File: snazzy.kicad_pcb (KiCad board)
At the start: 2 copper layers, 28 parts, among them J1 Conn_01x03, J2 Conn_01x03, SW1 BTN_START, SW10 BTN_DOWN, SW11 BTN_L, SW12 BTN_R, SW2 BTN_SELECT, SW3 BTN_A, SW4 BTN_B, SW5 BTN_X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

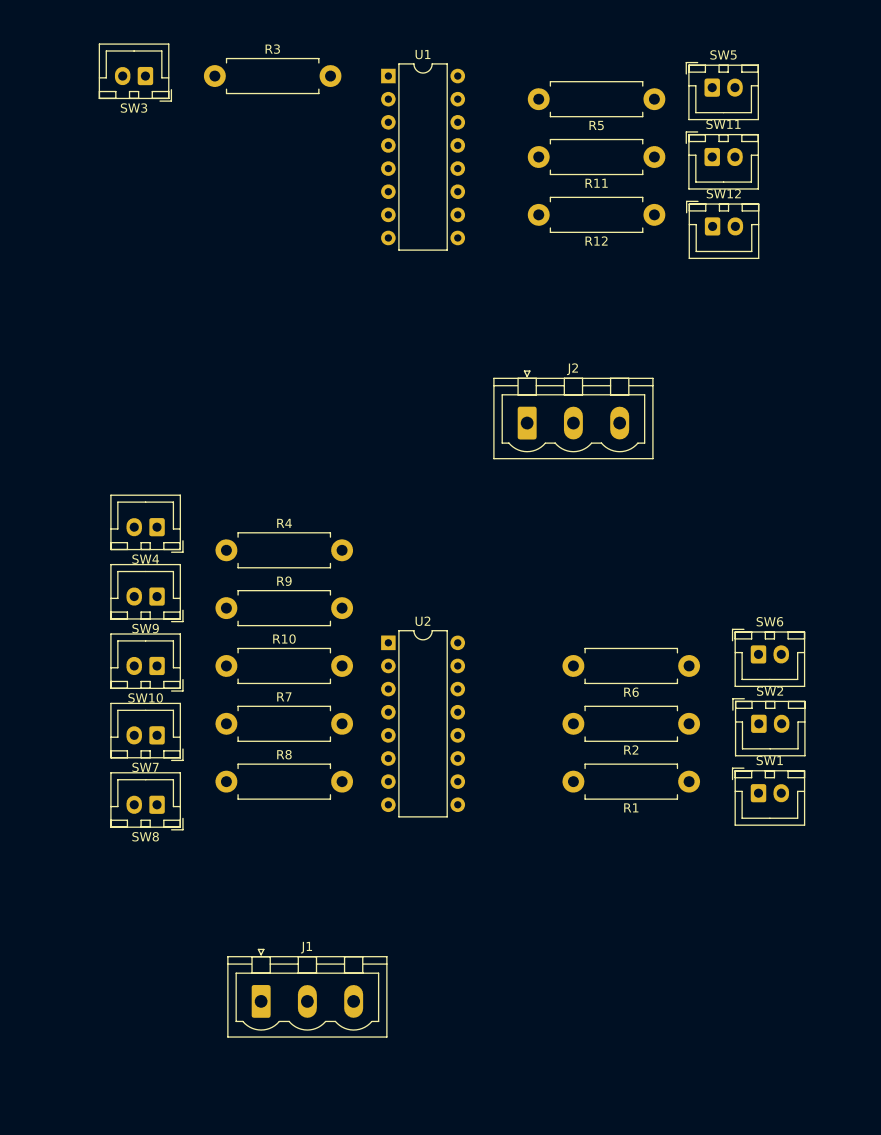
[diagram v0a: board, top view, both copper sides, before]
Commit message: Add traces to PCB components
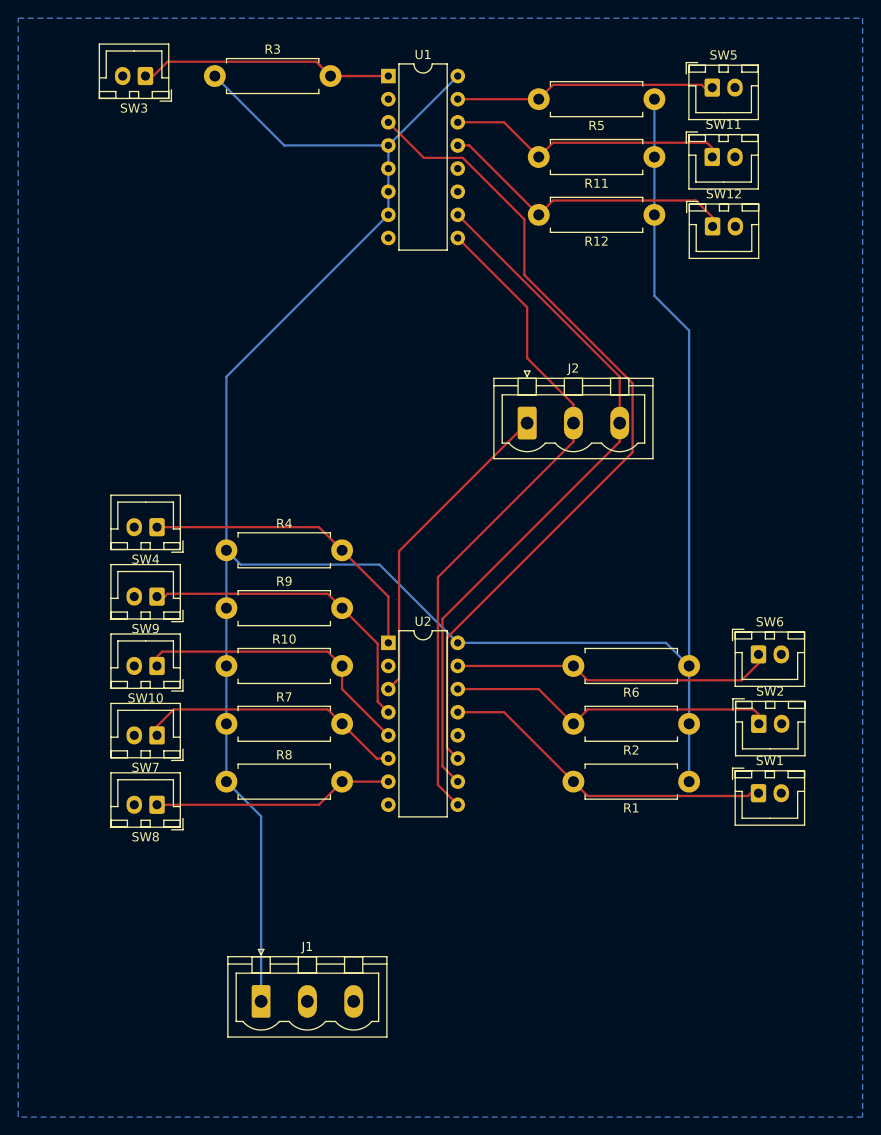
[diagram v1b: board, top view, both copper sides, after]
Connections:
- J2 pad 1: SNES_latch -> SNES_data1
- J2 pad 2: SNES_data1 -> SNES_latch
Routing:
- net +5V: track 0.00 -> 268.5 mm
- net Net-(U1-Pad3): track 0.00 -> 92.4 mm
- net SNES_clack: track 0.00 -> 78.3 mm
- net SNES_latch: track 0.00 -> 74.6 mm
- net /BTN_START: track 0.00 -> 37.0 mm
- net /BTN_SELECT: track 0.00 -> 36.5 mm
- net SNES_data1: track 0.00 -> 35.5 mm
- net /BTN_Y: track 0.00 -> 35.4 mm
- net /BTN_UP: track 0.00 -> 34.6 mm
- net /BTN_B: track 0.00 -> 33.6 mm
- net /BTN_R: track 0.00 -> 33.6 mm
- net /BTN_DOWN: track 0.00 -> 31.9 mm
- net /BTN_L: track 0.00 -> 31.4 mm
- net /BTN_LEFT: track 0.00 -> 29.4 mm
- net /BTN_X: track 0.00 -> 28.7 mm
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- added copper zone on B.Cu, net GND

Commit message: Optimize PCB footprint to save space
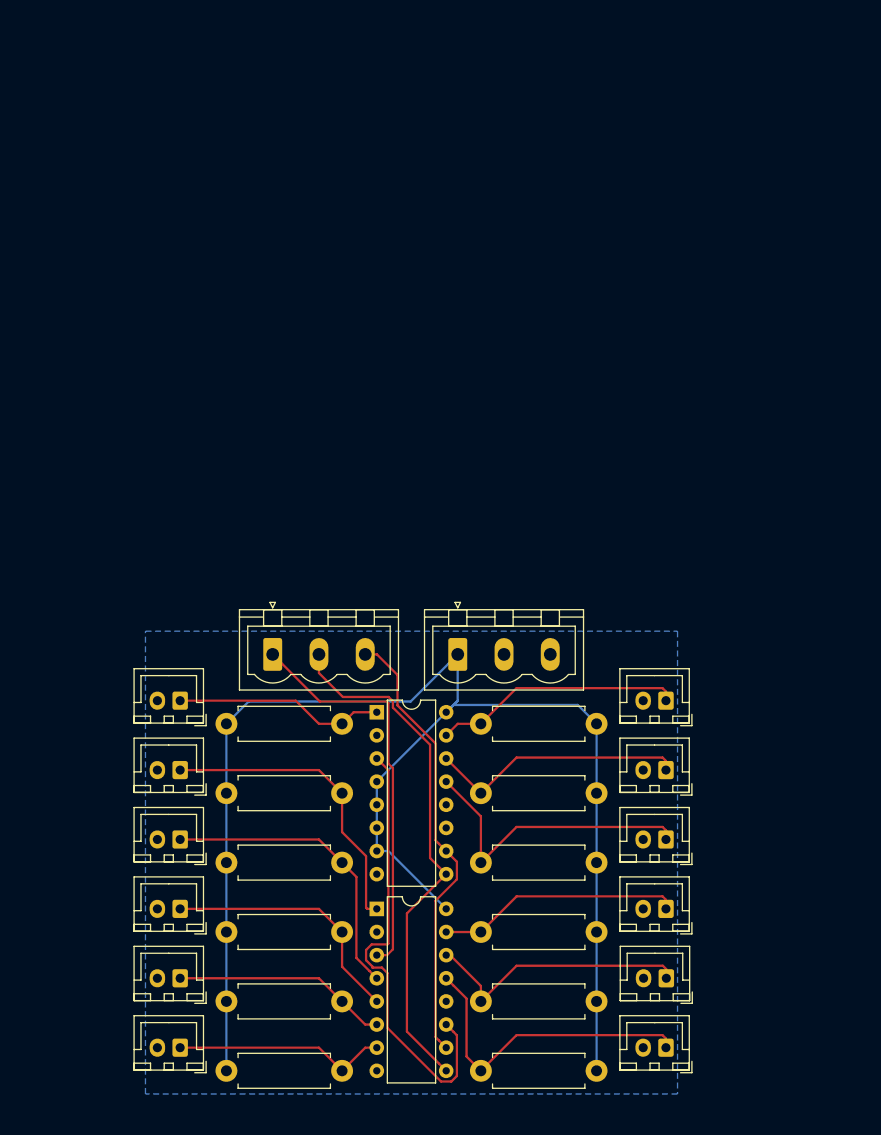
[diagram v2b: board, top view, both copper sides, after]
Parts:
- moved R12 71.4 mm to (161.3, 102.9)
- moved R3 71.1 mm to (120.7, 87.6)
- moved R11 70.1 mm to (161.3, 95.2)
- moved U1 69.9 mm to (137.2, 86.4)
- moved R5 68.9 mm to (161.3, 87.6)
- moved SW3 68.7 mm to (115.6, 85.1)
- moved SW12 67.5 mm to (168.9, 100.3), turned to 180 degrees
- moved SW11 67.5 mm to (168.9, 92.7), turned to 180 degrees
- moved SW5 67.5 mm to (168.9, 85.1), turned to 180 degrees
- moved J1 43.8 mm to (146.1, 80.0)
- moved J2 37.8 mm to (125.7, 80.0)
- moved R1 33.3 mm to (161.3, 125.7)
- moved R2 32.1 mm to (161.3, 118.1)
- moved R8 31.8 mm to (120.7, 125.7)
- moved R6 30.9 mm to (161.3, 110.5)
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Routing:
- net +5V: track 268.5 -> 159.8 mm
- net Net-(U1-Pad3): track 92.4 -> 50.2 mm
- net SNES_clack: track 78.3 -> 49.6 mm
- net SNES_latch: track 74.6 -> 58.0 mm
- net SNES_data1: track 35.5 -> 44.2 mm
- net /BTN_Y: track 35.4 -> 26.9 mm
- net /BTN_SELECT: track 36.5 -> 30.0 mm
- net /BTN_LEFT: track 29.4 -> 23.7 mm
- net /BTN_A: track 28.0 -> 23.2 mm
- net /BTN_DOWN: track 31.9 -> 28.0 mm
- net /BTN_L: track 31.4 -> 28.5 mm
- net /BTN_RIGHT: track 26.5 -> 23.7 mm
- net /BTN_START: track 37.0 -> 34.8 mm
- net /BTN_UP: track 34.6 -> 33.1 mm
- net /BTN_X: track 28.7 -> 27.4 mm

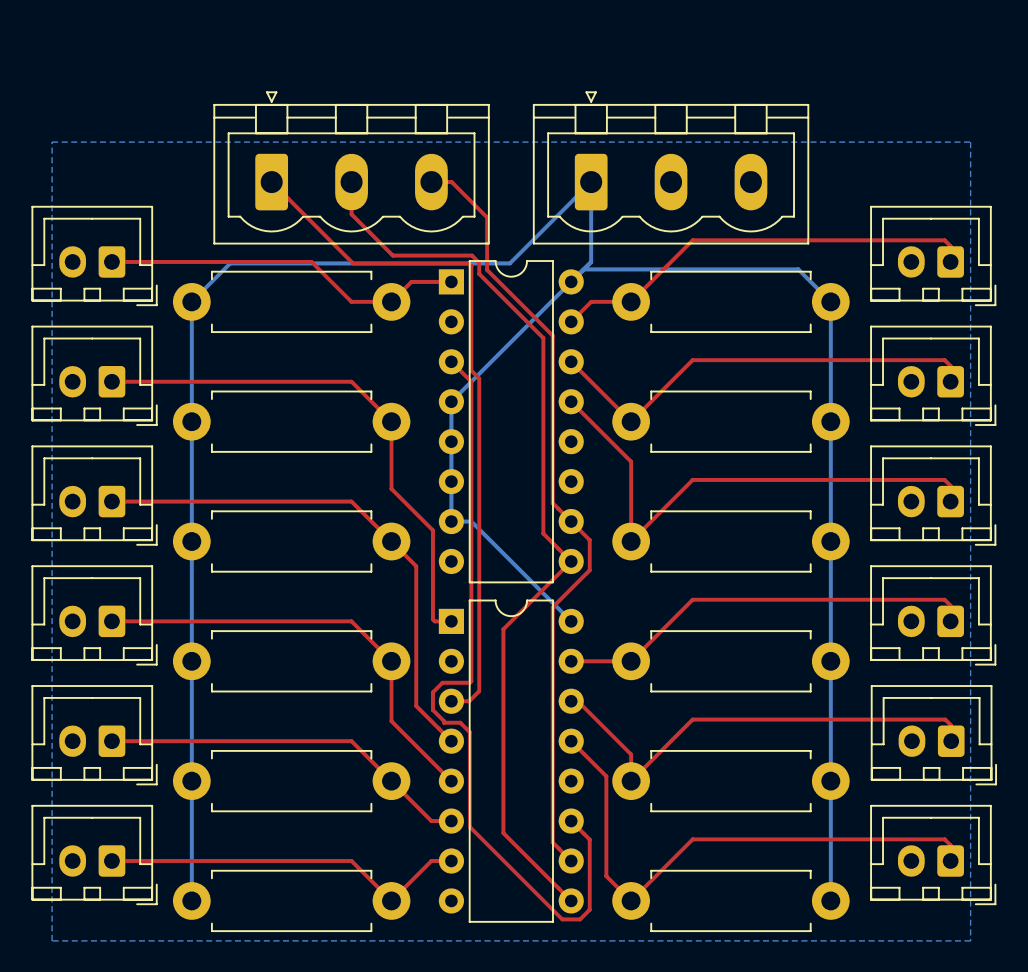
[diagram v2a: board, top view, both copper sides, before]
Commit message: Add capacitor to absorb IC voltage drops
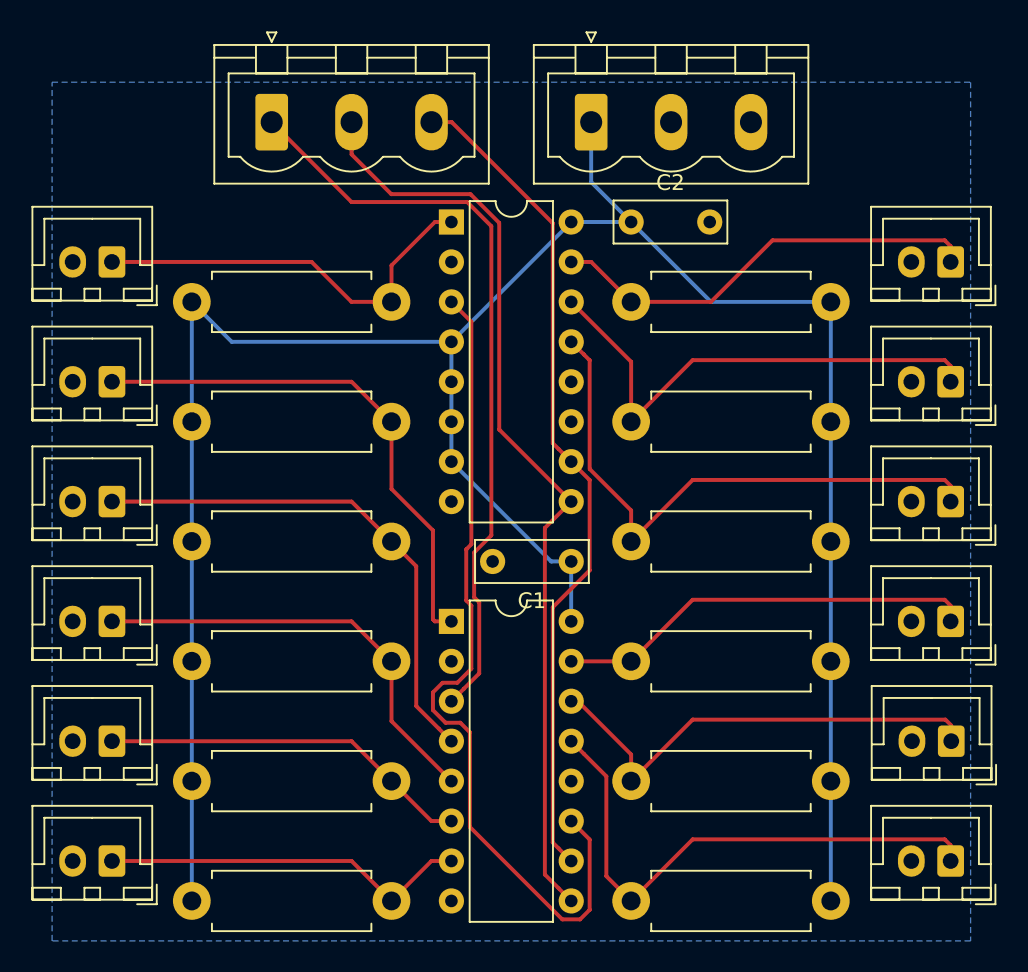
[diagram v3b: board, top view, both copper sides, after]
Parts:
- added C1: 100n, Capacitor_THT:C_Rect_L7.0mm_W2.5mm_P5.00mm, F.Cu at (144.8, 104.1)
- added C2: 100n, Capacitor_THT:C_Rect_L7.0mm_W2.5mm_P5.00mm, F.Cu at (148.6, 82.5)
- moved J1 3.81 mm to (146.1, 76.2)
- moved J2 3.81 mm to (125.7, 76.2)
- moved U1 3.81 mm to (137.2, 82.5)
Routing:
- net +5V: track 159.8 -> 152.2 mm
- net SNES_data1: track 44.2 -> 48.2 mm
- net SNES_clack: track 49.6 -> 53.4 mm
- net /BTN_R: track 33.6 -> 37.4 mm
- net /BTN_L: track 28.5 -> 32.3 mm
- net Net-(U1-Pad3): track 50.2 -> 53.7 mm
- net /BTN_A: track 23.2 -> 26.1 mm
- net SNES_latch: track 58.0 -> 59.7 mm
- net /BTN_X: track 27.4 -> 28.0 mm

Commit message: Update schematic and PCB (unsure what changed)
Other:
- board outline added: 66 x 59.7 mm
- board text added: "A"
- board text added: "B"
- board text added: "L"
- board text added: "R"
- board text added: "X"
- board text added: "Y"
- board text added: "down"
- board text added: "left"
- board text added: "right"
- board text added: "select"
- board text added: "start"
- board text added: "up"
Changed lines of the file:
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@@
   (general
     (thickness 1.6)
-    (drawings 0)
+    (drawings 23)
     (tracks 147)
     (zones 0)
@@
   )
   (layers
-    (0 F.Cu signal)
-    (31 B.Cu signal)
+    (0 F.Cu signal hide)
+    (31 B.Cu signal hide)
     (32 B.Adhes user)
     (33 F.Adhes user)
@@
     (descr "C, Rect series, Radial, pin pitch=5.00mm, , length*width=7*2.5mm^2, Capacitor")
     (tags "C Rect series Radial pin pitch 5.00mm  length 7mm width 2.5mm Capacitor")
-    (fp_text reference C2 (at 2.5 -2.5) (layer F.SilkS)
+    (fp_text reference C2 (at 2.5 -2.5) (layer F.SilkS) hide
       (effects (font (size 1 1) (thickness 0.15)))
     )
@@
     (descr "C, Rect series, Radial, pin pitch=5.00mm, , length*width=7*2.5mm^2, Capacitor")
     (tags "C Rect series Radial pin pitch 5.00mm  length 7mm width 2.5mm Capacitor")
-    (fp_text reference C1 (at 2.5 -2.5) (layer F.SilkS)
+    (fp_text reference C1 (at 2.5 -2.5) (layer F.SilkS) hide
       (effects (font (size 1 1) (thickness 0.15)))
     )
@@
     )
   )
+  (dimension 59.69 (width 0.15) (layer Dwgs.User)
+    (gr_text "59.690 mm" (at 89.505001 99.695 270) (layer Dwgs.User)
+      (effects (font (size 1 1) (thickness 0.15)))
+    )
+    (feature1 (pts (xy 107.95 129.54) (xy 90.21858 129.54)))
+    (feature2 (pts (xy 107.95 69.85) (xy 90.21858 69.85)))
+    (crossbar (pts (xy 90.805001 69.85) (xy 90.805001 129.54)))
+    (arrow1a (pts (xy 90.805001 129.54) (xy 90.21858 128.413496)))
+    (arrow1b (pts (xy 90.805001 129.54) (xy 91.391422 128.413496)))
+    (arrow2a (pts (xy 90.805001 69.85) (xy 90.21858 70.976504)))
+    (arrow2b (pts (xy 90.805001 69.85) (xy 91.391422 70.976504)))
+  )
+  (dimension 66.04 (width 0.15) (layer Dwgs.User)
+    (gr_text "66.040 mm" (at 140.97 53.31) (layer Dwgs.User)
+      (effects (font (size 1 1) (thickness 0.15)))
+    )
+    (feature1 (pts (xy 173.99 69.85) (xy 173.99 54.023579)))
+    (feature2 (pts (xy 107.95 69.85) (xy 107.95 54.023579)))
+    (crossbar (pts (xy 107.95 54.61) (xy 173.99 54.61)))
+    (arrow1a (pts (xy 173.99 54.61) (xy 172.863496 55.196421)))
+    (arrow1b (pts (xy 173.99 54.61) (xy 172.863496 54.023579)))
+    (arrow2a (pts (xy 107.95 54.61) (xy 109.076504 55.196421)))
+    (arrow2b (pts (xy 107.95 54.61) (xy 109.076504 54.023579)))
+  )
+  (gr_line (start 109.22 69.85) (end 107.95 69.85) (layer Edge.Cuts) (width 0.05))
+  (gr_line (start 173.99 128.905) (end 173.99 129.54) (layer Edge.Cuts) (width 0.05))
+  (gr_line (start 109.22 129.54) (end 107.95 129.54) (layer Edge.Cuts) (width 0.05))
+  (gr_text right (at 109.22 122.555 90) (layer F.SilkS)
+    (effects (font (size 1 1) (thickness 0.15)))
+  )
+  (gr_text left (at 109.22 114.935 90) (layer F.SilkS)
+    (effects (font (size 1 1) (thickness 0.15)))
+  )
+  (gr_text down (at 109.22 107.315 90) (layer F.SilkS)
+    (effects (font (size 1 1) (thickness 0.15)))
+  )
+  (gr_text up (at 109.22 99.695 90) (layer F.SilkS)
+    (effects (font (size 1 1) (thickness 0.15)))
+  )
+  (gr_text B (at 109.22 92.075 90) (layer F.SilkS)
+    (effects (font (size 1 1) (thickness 0.15)))
+  )
+  (gr_text A (at 109.22 84.455 90) (layer F.SilkS)
+    (effects (font (size 1 1) (thickness 0.15)))
+  )
+  (gr_text start (at 172.72 122.555 270) (layer F.SilkS)
+    (effects (font (size 1 1) (thickness 0.15)))
+  )
+  (gr_text select (at 172.72 114.935 270) (layer F.SilkS)
+    (effects (font (size 1 1) (thickness 0.15)))
+  )
+  (gr_text Y (at 172.72 107.315 270) (layer F.SilkS)
+    (effects (font (size 1 1) (thickness 0.15)))
+  )
+  (gr_text R (at 172.72 99.695 270) (layer F.SilkS)
+    (effects (font (size 1 1) (thickness 0.15)))
+  )
+  (gr_text L (at 172.72 92.075 270) (layer F.SilkS)
+    (effects (font (size 1 1) (thickness 0.15)))
+  )
+  (gr_text X (at 172.72 84.455 270) (layer F.SilkS)
+    (effects (font (size 1 1) (thickness 0.15)))
+  )
+  (gr_line (start 173.99 129.54) (end 172.72 129.54) (layer Edge.Cuts) (width 0.05))
+  (gr_line (start 173.99 69.85) (end 172.72 69.85) (layer Edge.Cuts) (width 0.05))
+  (gr_line (start 107.95 129.54) (end 107.95 69.85) (layer Edge.Cuts) (width 0.05))
+  (gr_line (start 172.72 129.54) (end 109.22 129.54) (layer Edge.Cuts) (width 0.05))
+  (gr_line (start 173.99 69.85) (end 173.99 128.905) (layer Edge.Cuts) (width 0.05))
+  (gr_line (start 109.22 69.85) (end 172.72 69.85) (layer Edge.Cuts) (width 0.05))
   (segment (start 161.29 87.63) (end 161.29 95.25) (width 0.25) (layer B.Cu) (net 3))
   (segment (start 161.29 95.25) (end 161.29 102.87) (width 0.25) (layer B.Cu) (net 3))
@@
     (polygon
       (pts
-        (xy 170.18 128.27) (xy 111.76 128.27) (xy 111.76 73.66) (xy 170.18 73.66)
+        (xy 173.99 129.54) (xy 107.95 129.54) (xy 107.95 69.85) (xy 173.99 69.85)
       )
     )
